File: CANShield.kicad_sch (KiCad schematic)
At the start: 93 parts, among them J101 Conn_02x19_Odd_Even, J102 Conn_02x19_Odd_Even, J103 Conn_01x04_Socket, J104 Conn_01x06_Socket, Q101 Si1308EDL, Q102 Si1308EDL, Q103 Si1308EDL, U101 TJA1443ATK/0Z, U102 BD2222G, U103 AT25SF081-XMHD-X, U104 MR20H40

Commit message: working on PCB
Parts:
- removed TP110, TP111: TestPoint_Small, TestPoint:TestPoint_Pad_D1.0mm, symbol Connector:TestPoint_Small
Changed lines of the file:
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@@
 	)
 	(junction
-		(at 125.73 229.87)
-		(diameter 0)
-		(color 0 0 0 0)
-	)
-	(junction
 		(at 133.35 196.85)
 		(diameter 0)
@@
 	)
 	(junction
-		(at 125.73 237.49)
-		(diameter 0)
-		(color 0 0 0 0)
-	)
-	(junction
 		(at 157.48 237.49)
 		(diameter 0)
@@
 	(wire
 		(pts
-			(xy 121.92 237.49) (xy 125.73 237.49)
+			(xy 121.92 237.49) (xy 157.48 237.49)
 		)
 		(stroke
@@
 	(wire
 		(pts
-			(xy 105.41 229.87) (xy 125.73 229.87)
+			(xy 105.41 229.87) (xy 137.16 229.87)
 		)
 		(stroke
@@
 	(wire
 		(pts
-			(xy 125.73 229.87) (xy 137.16 229.87)
-		)
-		(stroke
-			(width 0)
-			(type default)
-		)
-	)
-	(wire
-		(pts
 			(xy 143.51 196.85) (xy 142.24 196.85)
 		)
@@
 	(wire
 		(pts
-			(xy 125.73 237.49) (xy 157.48 237.49)
-		)
-		(stroke
-			(width 0)
-			(type default)
-		)
-	)
-	(wire
-		(pts
 			(xy 323.85 110.49) (xy 342.9 110.49)
 		)
@@
 	)
 	(symbol
-		(lib_id "Connector:TestPoint_Small")
-		(at 125.73 229.87 0)
-		(unit 1)
-		(exclude_from_sim no)
-		(in_bom yes)
-		(on_board yes)
-		(dnp no)
-		(property "Reference" "TP110"
-			(at 123.952 228.346 0)
-			(effects
-				(font
-					(size 1.27 1.27)
-				)
-				(justify left)
-			)
-		)
-		(property "Value" "TestPoint_Small"
-			(at 127 231.1399 0)
-			(effects
-				(font
-					(size 1.27 1.27)
-				)
-				(justify left)
-				(hide yes)
-			)
-		)
-		(property "Footprint" "TestPoint:TestPoint_Pad_D1.0mm"
-			(at 130.81 229.87 0)
-			(effects
-				(font
-					(size 1.27 1.27)
-				)
-				(hide yes)
-			)
-		)
-		(property "Datasheet" "~"
-			(at 130.81 229.87 0)
-			(effects
-				(font
-					(size 1.27 1.27)
-				)
-				(hide yes)
-			)
-		)
-		(property "Description" "test point"
-			(at 125.73 229.87 0)
-			(effects
-				(font
-					(size 1.27 1.27)
-				)
-				(hide yes)
-			)
-		)
-		(pin "1"
-		)
-		(instances
-			(project "CANShield"
-				(path "/b267ac6b-6338-40f7-a3df-596945dc6f78"
-					(reference "TP110")
-					(unit 1)
-				)
-			)
-		)
-	)
-	(symbol
 		(lib_id "Device:R")
 		(at 342.9 101.6 0)
@@
 					(unit 1)
 				)
-			)
-		)
-	)
-	(symbol
-		(lib_id "Connector:TestPoint_Small")
-		(at 125.73 237.49 0)
-		(unit 1)
-		(exclude_from_sim no)
-		(in_bom yes)
-		(on_board yes)
-		(dnp no)
-		(property "Reference" "TP111"
-			(at 123.952 235.966 0)
-			(effects
-				(font
-					(size 1.27 1.27)
-				)
-				(justify left)
-			)
-		)
-		(property "Value" "TestPoint_Small"
-			(at 127 238.7599 0)
-			(effects
-				(font
-					(size 1.27 1.27)
-				)
-				(justify left)
-				(hide yes)
-			)
-		)
-		(property "Footprint" "TestPoint:TestPoint_Pad_D1.0mm"
-			(at 130.81 237.49 0)
-			(effects
-				(font
-					(size 1.27 1.27)
-				)
-				(hide yes)
-			)
-		)
-		(property "Datasheet" "~"
-			(at 130.81 237.49 0)
-			(effects
-				(font
-					(size 1.27 1.27)
-				)
-				(hide yes)
-			)
-		)
-		(property "Description" "test point"
-			(at 125.73 237.49 0)
-			(effects
-				(font
-					(size 1.27 1.27)
-				)
-				(hide yes)
-			)
-		)
-		(pin "1"
-		)
-		(instances
-			(project "CANShield"
-				(path "/b267ac6b-6338-40f7-a3df-596945dc6f78"
-					(reference "TP111")
-					(unit 1)
-				)

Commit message: Add BOM to project
Add BOM and did Gerber Data
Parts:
- C101, C102, C103, C104, C105, C106, C107, C108, C109, C110, C111, C112, C113, C114, CR101, CR102, D101, D102, D103, D104, FID101, FID102, FID103, H101, H102, H103, J101, J102, J103, J104, JP101, JP102, JP103, JP104, L101, L102, L103, L104, L105, L106, L107, Q101, Q102, Q103, R101, R102, R103, R104, R105, R106, R107, R108, R109, R110, R111, R112, R113, R114, R115, R116, R117, R118, R119, R120, R121, R122, R123, R124, R125, R126, TP101, TP102, TP103, TP104, TP105, TP106, TP107, TP108, TP109, TP112, TP113, TP114, TP115, TP116, TP117, TP118, TP119, U101, U102, U103, U104: JLCPCB Part # (optional) (none) -> ${ITEM_NUMBER}

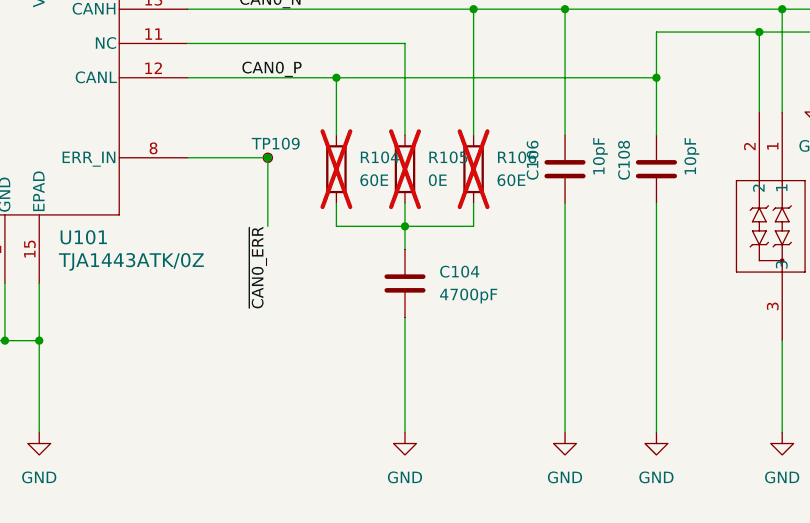
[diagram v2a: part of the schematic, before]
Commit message: Update BOM
Small changes on pcb layout and update BOM
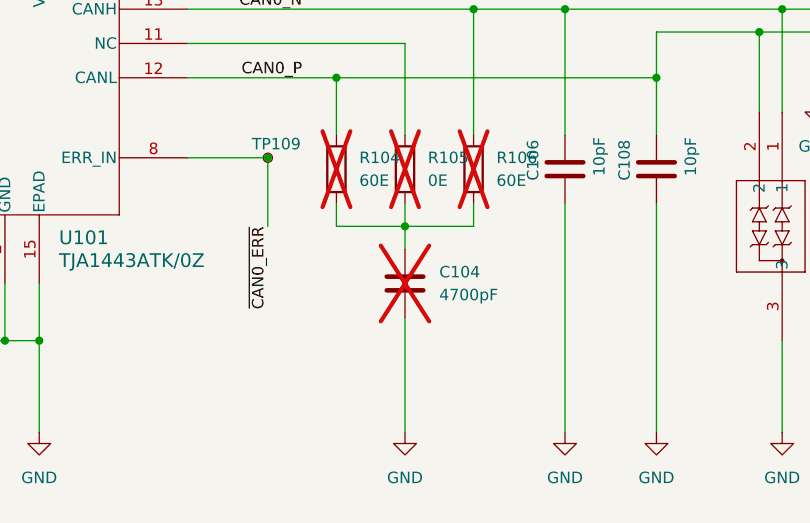
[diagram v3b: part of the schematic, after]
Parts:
- C104: now not fitted; now left out of the parts list
- C114, R102, R104, R105, R106, R118, R119, R122, R124, R125, R126, TP102, TP103, TP104, TP105, TP107, TP109, TP112, TP113, TP115, TP116, TP117, TP118, TP119, U104: now left out of the parts list
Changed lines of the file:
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@@
 		(unit 1)
 		(exclude_from_sim no)
-		(in_bom yes)
+		(in_bom no)
 		(on_board yes)
 		(dnp no)
@@
 		(unit 1)
 		(exclude_from_sim no)
-		(in_bom yes)
+		(in_bom no)
 		(on_board yes)
 		(dnp no)
@@
 		(unit 1)
 		(exclude_from_sim no)
-		(in_bom yes)
+		(in_bom no)
 		(on_board yes)
 		(dnp yes)
@@
 		(unit 1)
 		(exclude_from_sim no)
-		(in_bom yes)
+		(in_bom no)
 		(on_board yes)
 		(dnp no)
@@
 		(unit 1)
 		(exclude_from_sim no)
-		(in_bom yes)
+		(in_bom no)
 		(on_board yes)
 		(dnp yes)
@@
 		(unit 1)
 		(exclude_from_sim no)
-		(in_bom yes)
+		(in_bom no)
 		(on_board yes)
 		(dnp yes)
@@
 		(unit 1)
 		(exclude_from_sim no)
-		(in_bom yes)
+		(in_bom no)
 		(on_board yes)
 		(dnp no)
@@
 		(unit 1)
 		(exclude_from_sim no)
-		(in_bom yes)
+		(in_bom no)
 		(on_board yes)
 		(dnp yes)
@@
 		(unit 1)
 		(exclude_from_sim no)
-		(in_bom yes)
+		(in_bom no)
 		(on_board yes)
 		(dnp no)
@@
 		(unit 1)
 		(exclude_from_sim no)
-		(in_bom yes)
+		(in_bom no)
 		(on_board yes)
 		(dnp no)
@@
 		(unit 1)
 		(exclude_from_sim no)
-		(in_bom yes)
+		(in_bom no)
 		(on_board yes)
 		(dnp yes)
@@
 		(unit 1)
 		(exclude_from_sim no)
-		(in_bom yes)
+		(in_bom no)
 		(on_board yes)
 		(dnp yes)
@@
 		(unit 1)
 		(exclude_from_sim no)
-		(in_bom yes)
+		(in_bom no)
 		(on_board yes)
 		(dnp yes)
@@
 		(unit 1)
 		(exclude_from_sim no)
-		(in_bom yes)
+		(in_bom no)
 		(on_board yes)
 		(dnp yes)
@@
 		(unit 1)
 		(exclude_from_sim no)
-		(in_bom yes)
+		(in_bom no)
 		(on_board yes)
 		(dnp yes)
@@
 		(unit 1)
 		(exclude_from_sim no)
-		(in_bom yes)
+		(in_bom no)
 		(on_board yes)
 		(dnp no)
@@
 		(unit 1)
 		(exclude_from_sim no)
-		(in_bom yes)
+		(in_bom no)
 		(on_board yes)
 		(dnp no)
@@
 		(unit 1)
 		(exclude_from_sim no)
-		(in_bom yes)
+		(in_bom no)
 		(on_board yes)
 		(dnp no)
@@
 		(unit 1)
 		(exclude_from_sim no)
-		(in_bom yes)
+		(in_bom no)
 		(on_board yes)
 		(dnp no)
@@
 		(unit 1)
 		(exclude_from_sim no)
-		(in_bom yes)
+		(in_bom no)
 		(on_board yes)
 		(dnp no)
@@
 		(unit 1)
 		(exclude_from_sim no)
-		(in_bom yes)
+		(in_bom no)
 		(on_board yes)
 		(dnp yes)
@@
 		(unit 1)
 		(exclude_from_sim no)
-		(in_bom yes)
+		(in_bom no)
 		(on_board yes)
 		(dnp yes)
@@
 		(unit 1)
 		(exclude_from_sim no)
-		(in_bom yes)
+		(in_bom no)
 		(on_board yes)
-		(dnp no)
+		(dnp yes)
 		(fields_autoplaced yes)
 		(property "Reference" "C104"
@@
 		(unit 1)
 		(exclude_from_sim no)
-		(in_bom yes)
+		(in_bom no)
 		(on_board yes)
 		(dnp no)
@@
 		(unit 1)
 		(exclude_from_sim no)
-		(in_bom yes)
+		(in_bom no)
 		(on_board yes)
 		(dnp yes)
@@
 		(unit 1)
 		(exclude_from_sim no)
-		(in_bom yes)
+		(in_bom no)
 		(on_board yes)
 		(dnp no)

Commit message: Update CANShield.kicad_sch
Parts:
- R116: value 1k -> 680
- R123: value 1k -> 340
- U102: value BD2222G -> BD22441G-C; JLCPCB Part # (optional) ${ITEM_NUMBER} -> C5576416
- U103: value AT25SF081-XMHD-X -> AT25DF041B-XMHNHR-T
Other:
- note added: "4Mbit NOR-Flash Memory to save firmware update Optional: 4Mbit SDRAM to save firmware for firmware update"
- note removed: "8Mbit NOR-Flash Memory to save firmware update Optional: 4MB SDRAM to save firmware for firmware update"
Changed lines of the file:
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@@
 		)
 	)
-	(text "8Mbit NOR-Flash Memory to save firmware update\nOptional: 4MB SDRAM to save firmware for firmware update\n"
+	(text "4Mbit NOR-Flash Memory to save firmware update\nOptional: 4Mbit SDRAM to save firmware for firmware update\n"
 		(exclude_from_sim no)
 		(at 281.178 72.898 0)
@@
 			)
 		)
-		(property "Value" "BD2222G"
+		(property "Value" "BD22441G-C"
 			(at 254 124.46 0)
 			(effects
@@
 			)
 		)
-		(property "Datasheet" "https://fscdn.rohm.com/en/products/databook/datasheet/ic/power/power_switch/bd2242g-e.pdf"
+		(property "Datasheet" "https://fscdn.rohm.com/en/products/databook/datasheet/ic/power/power_switch/bd22441g-c-e.pdf"
 			(at 254.254 150.876 0)
 			(effects
@@
 			)
 		)
-		(property "JLCPCB Part # (optional)" "${ITEM_NUMBER}"
+		(property "JLCPCB Part # (optional)" "C5576416"
 			(at 254 132.08 0)
 			(effects
@@
 			)
 		)
-		(property "Value" "AT25SF081-XMHD-X"
+		(property "Value" "AT25DF041B-XMHNHR-T"
 			(at 264.16 54.6099 0)
 			(effects
@@
 			)
 		)
-		(property "Datasheet" "https://www.adestotech.com/wp-content/uploads/DS-AT25SF081_045.pdf"
+		(property "Datasheet" "https://www.renesas.com/us/en/document/dst/at25df041b-datasheet?r=1608456"
 			(at 273.05 53.34 0)
 			(effects
@@
 			)
 		)
-		(property "Description" "8-Mbit, 2.5V Minimum SPI Serial Flash Memory with Dual-I/O and Quad-I/O Support, TSSOP-8"
+		(property "Description" "4-Mbit, 1.65 V Minimum SPI Serial Flash Memory with Dual I/O Support, TSSOP-8"
 			(at 273.05 53.34 0)
 			(effects
@@
 			)
 		)
-		(property "Value" "1k"
+		(property "Value" "680"
 			(at 309.88 213.3599 0)
 			(effects
@@
 			)
 		)
-		(property "Value" "1k"
+		(property "Value" "340"
 			(at 351.79 213.3599 0)
 			(effects

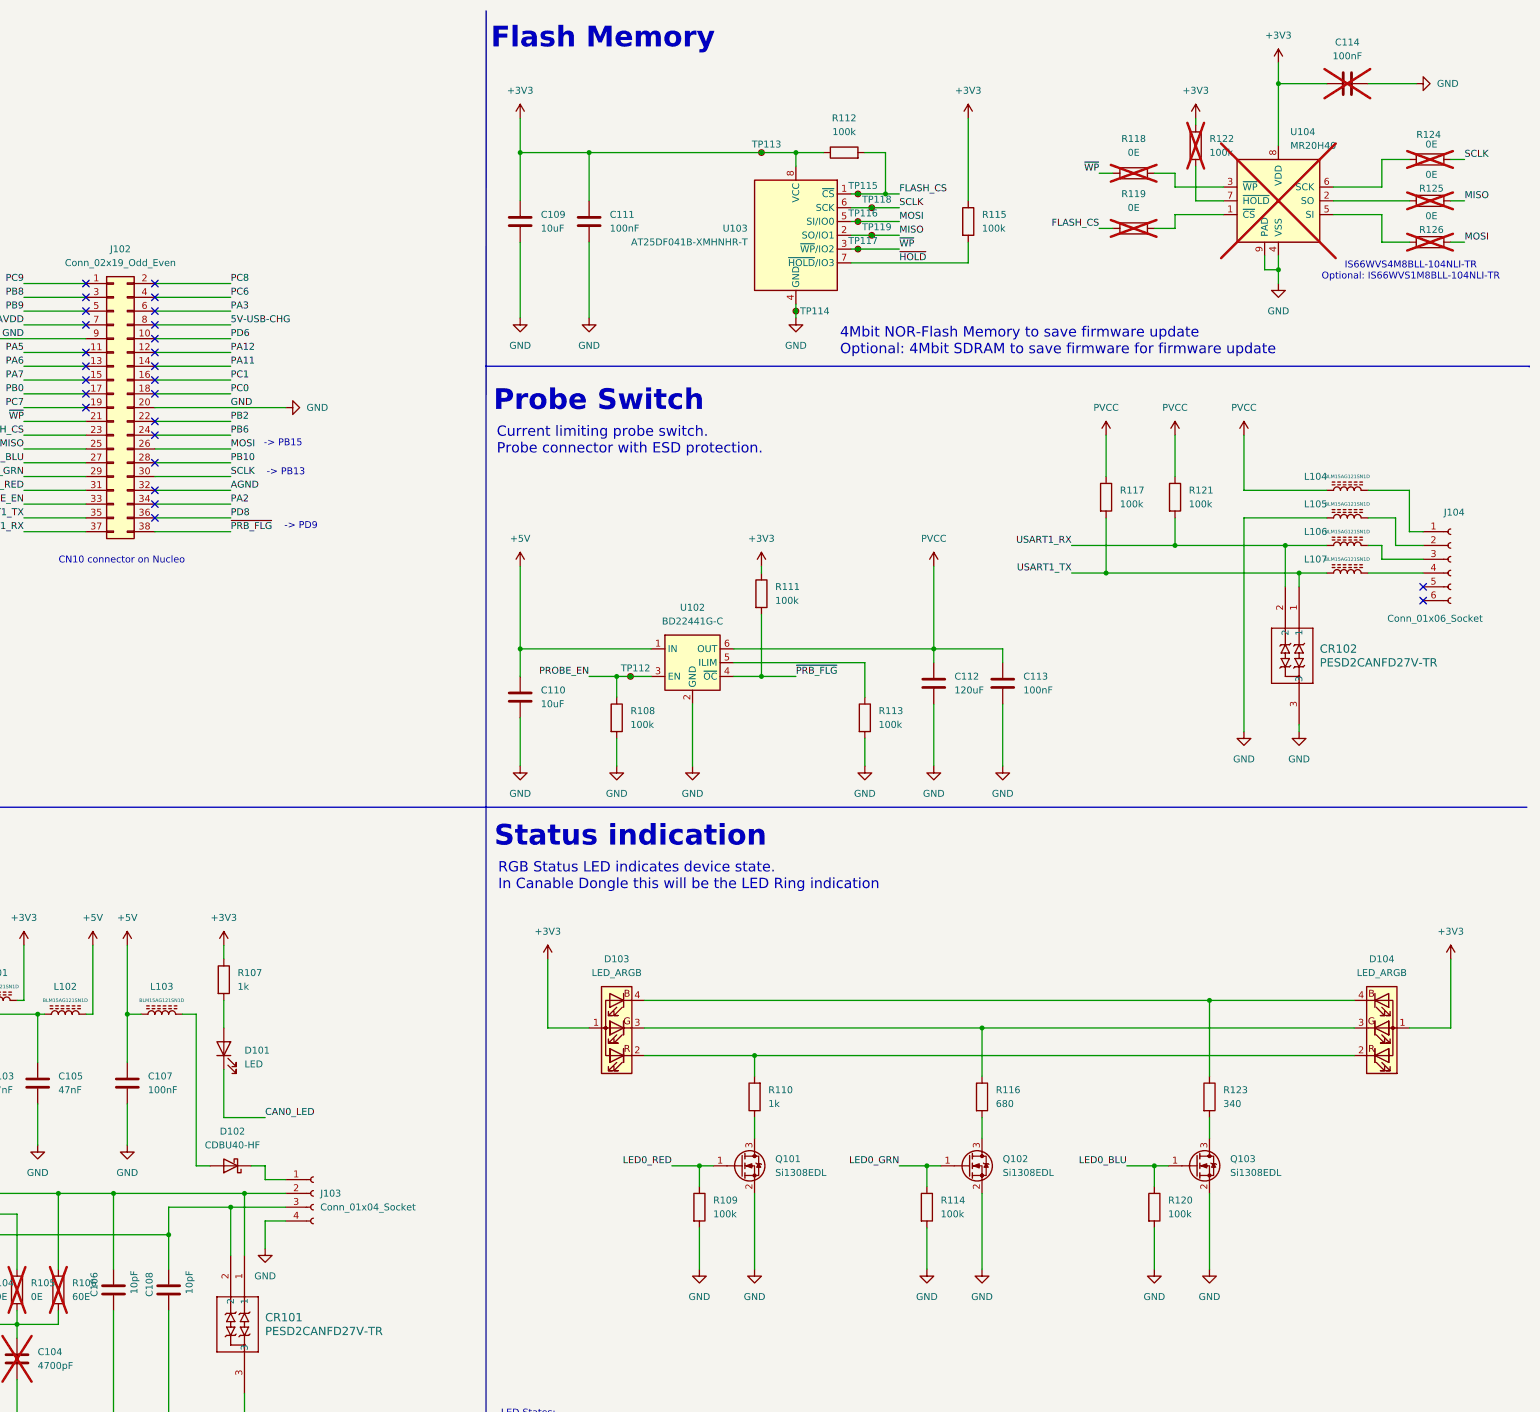
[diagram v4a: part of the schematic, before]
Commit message: Add bew esd diode
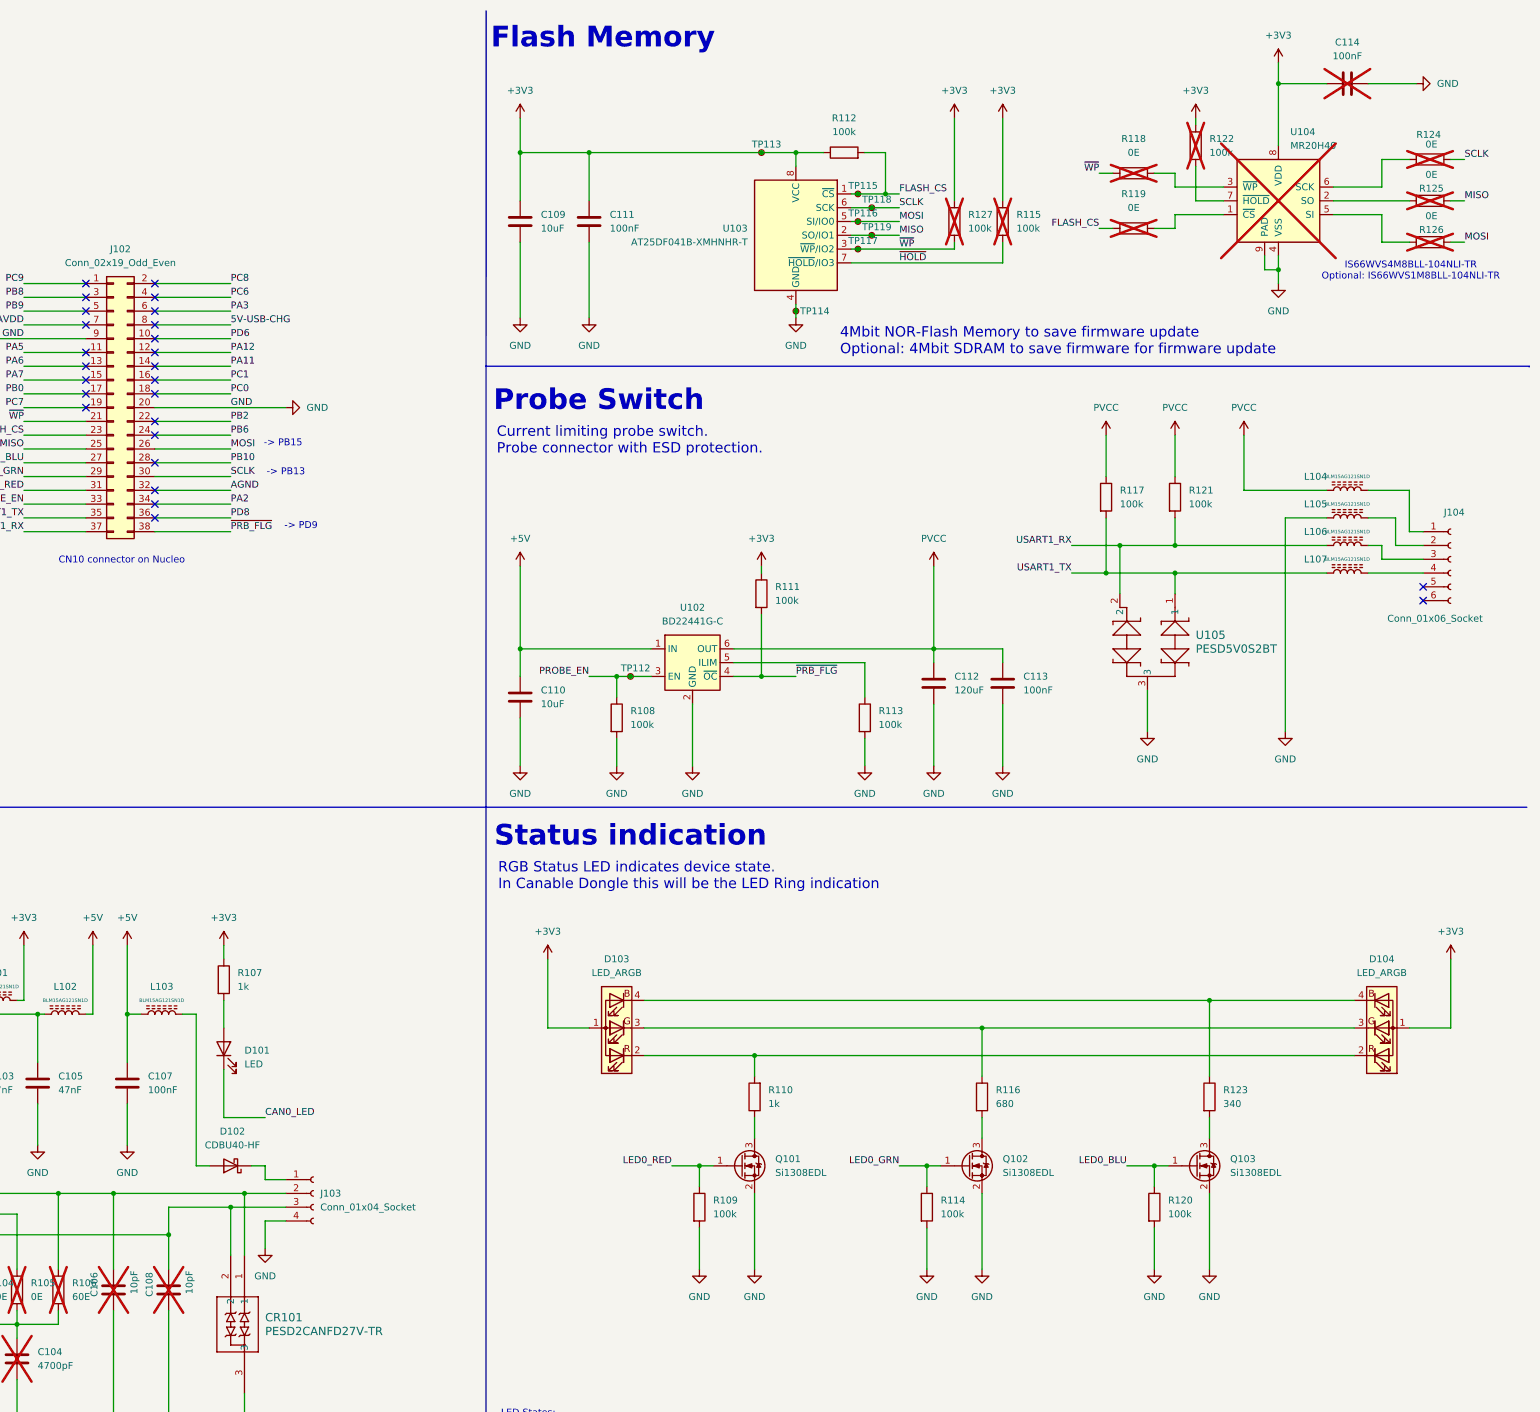
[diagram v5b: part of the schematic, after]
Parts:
- removed CR102: PESD2CANFD27V-TR, PESD2CANFD27V-TR:SOT23_PESD2_NEX, symbol PESD2CANFD27V:PESD2CANFD27V-TR
- added R127: 100k, Resistor_SMD:R_0402_1005Metric_Pad0.72x0.64mm_HandSolder, symbol Device:R
- added U105: PESD5V0S2BT, SOT23_NEX, symbol PESD5V0S2BT:PESD5V0S2BT
- C106, C108, R115: now not fitted; now left out of the parts list
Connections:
- net +3V3: now also R127.1
- net GND: now also U105.3
- net USART1_RX: now also U105.2
- net USART1_TX: now also U105.1
- net ~{WP}: now also R127.2

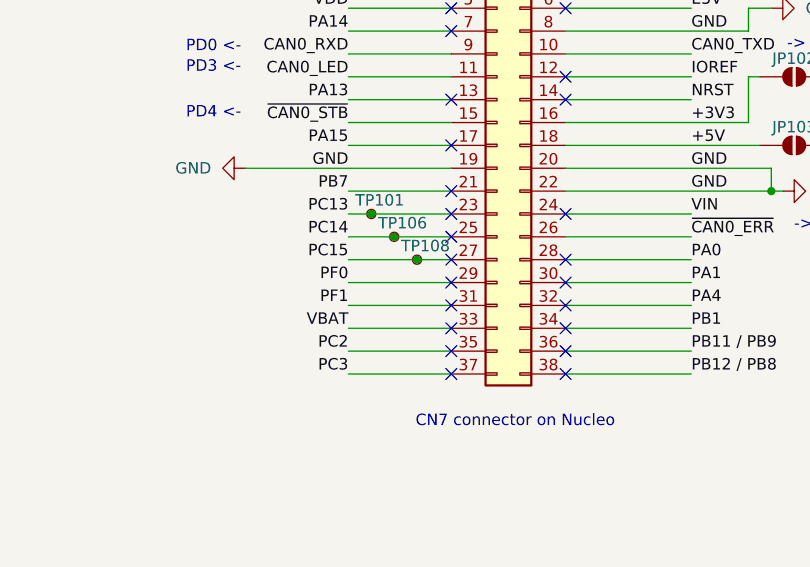
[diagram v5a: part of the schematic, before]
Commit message: Moved Testpoints
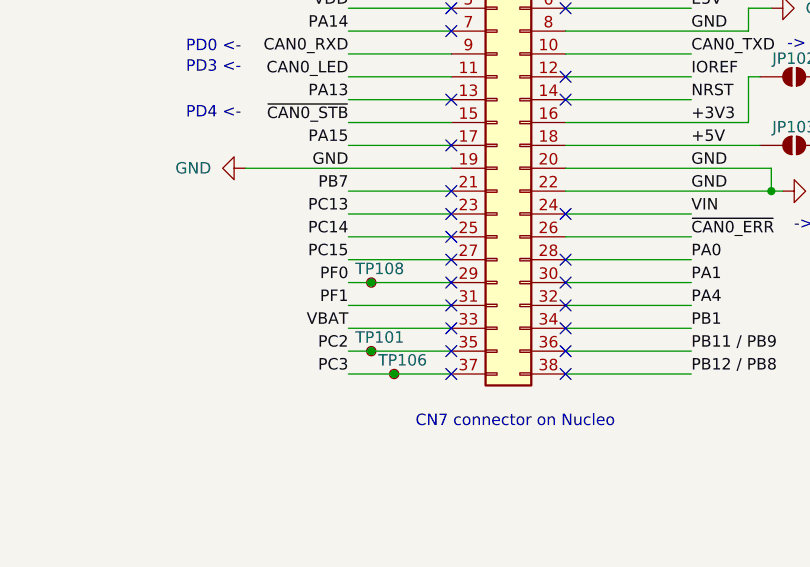
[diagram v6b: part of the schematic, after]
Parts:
- U105: footprint SOT23_NEX -> PESD5V:SOT23_NEX
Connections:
- net PC13: no longer TP101.1
- net PC14: no longer TP106.1
- net PC15: no longer TP108.1
- net PC2: now also TP101.1
- net PC3: now also TP106.1
- net PF0: now also TP108.1
